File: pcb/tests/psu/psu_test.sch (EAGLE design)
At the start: 26 parts, among them J1 CUI-PJ-013C, J2 SNG-100-HEADER-05-HDR-V, J3 SNG-100-HEADER-04-HDR-V, J4 SNG-100-HEADER-03-HDR-V, U1 ADP2303ARDZ, U2 TPS62086RLT, U3 TS4040D30IDBZ

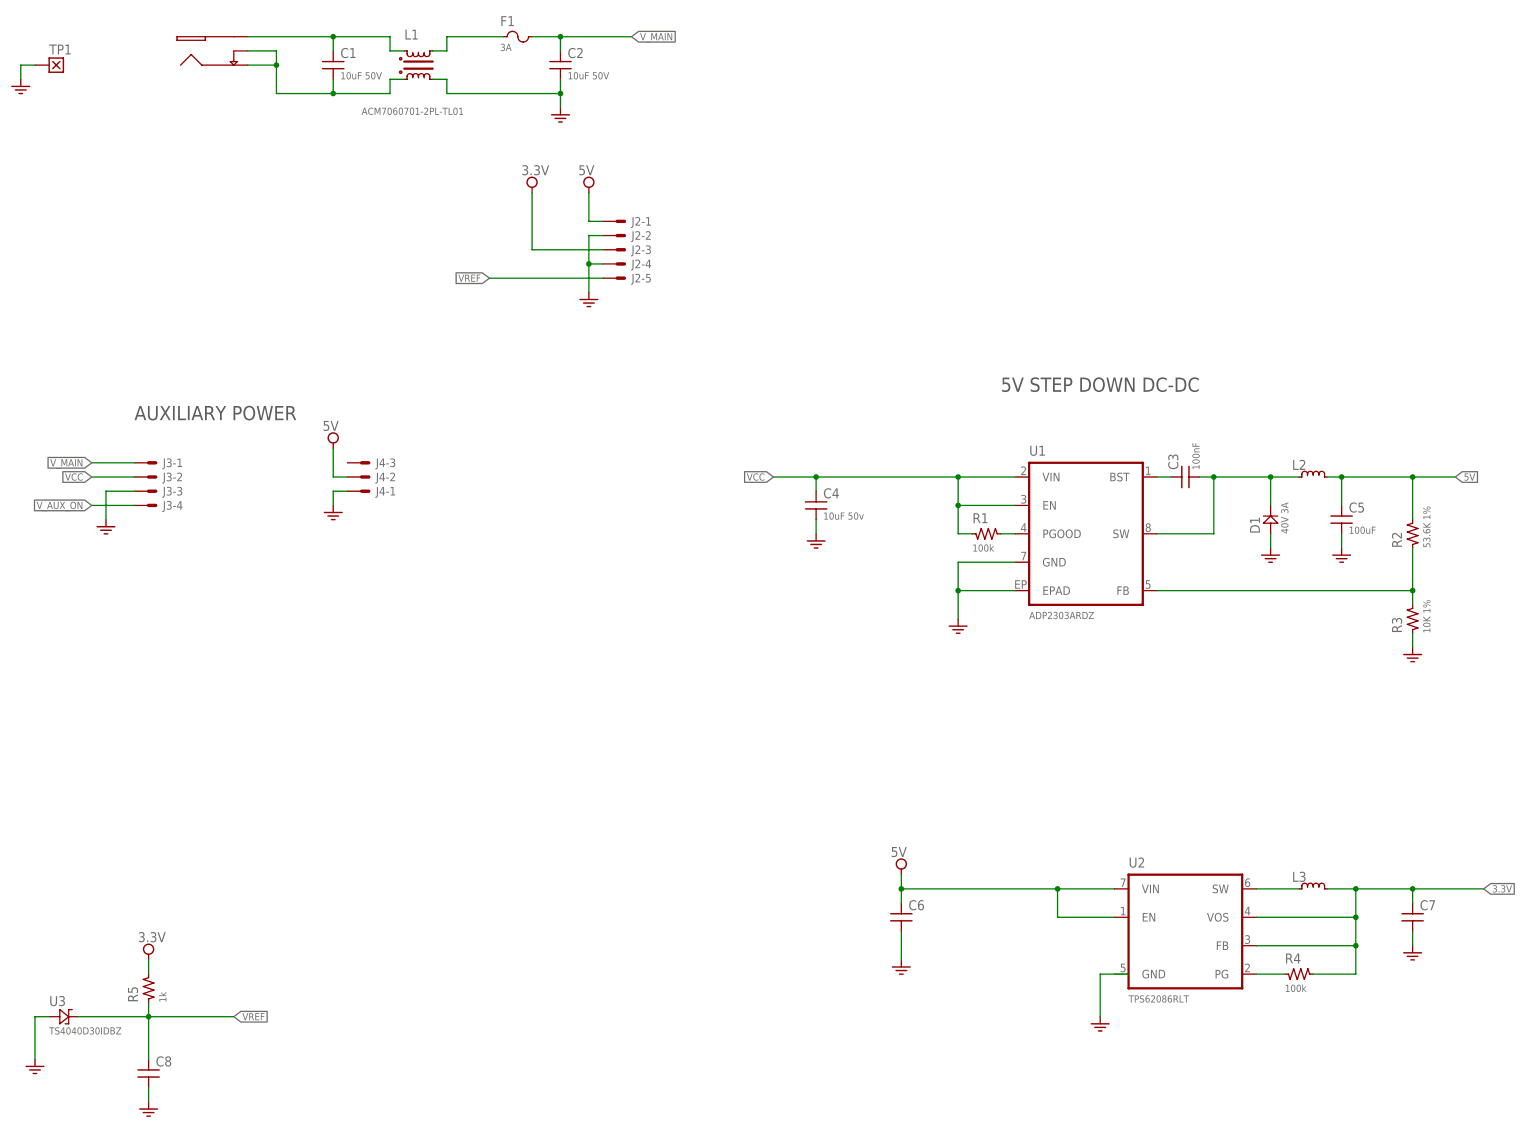
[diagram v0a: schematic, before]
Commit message: Corrected drawings of touch panel PCB
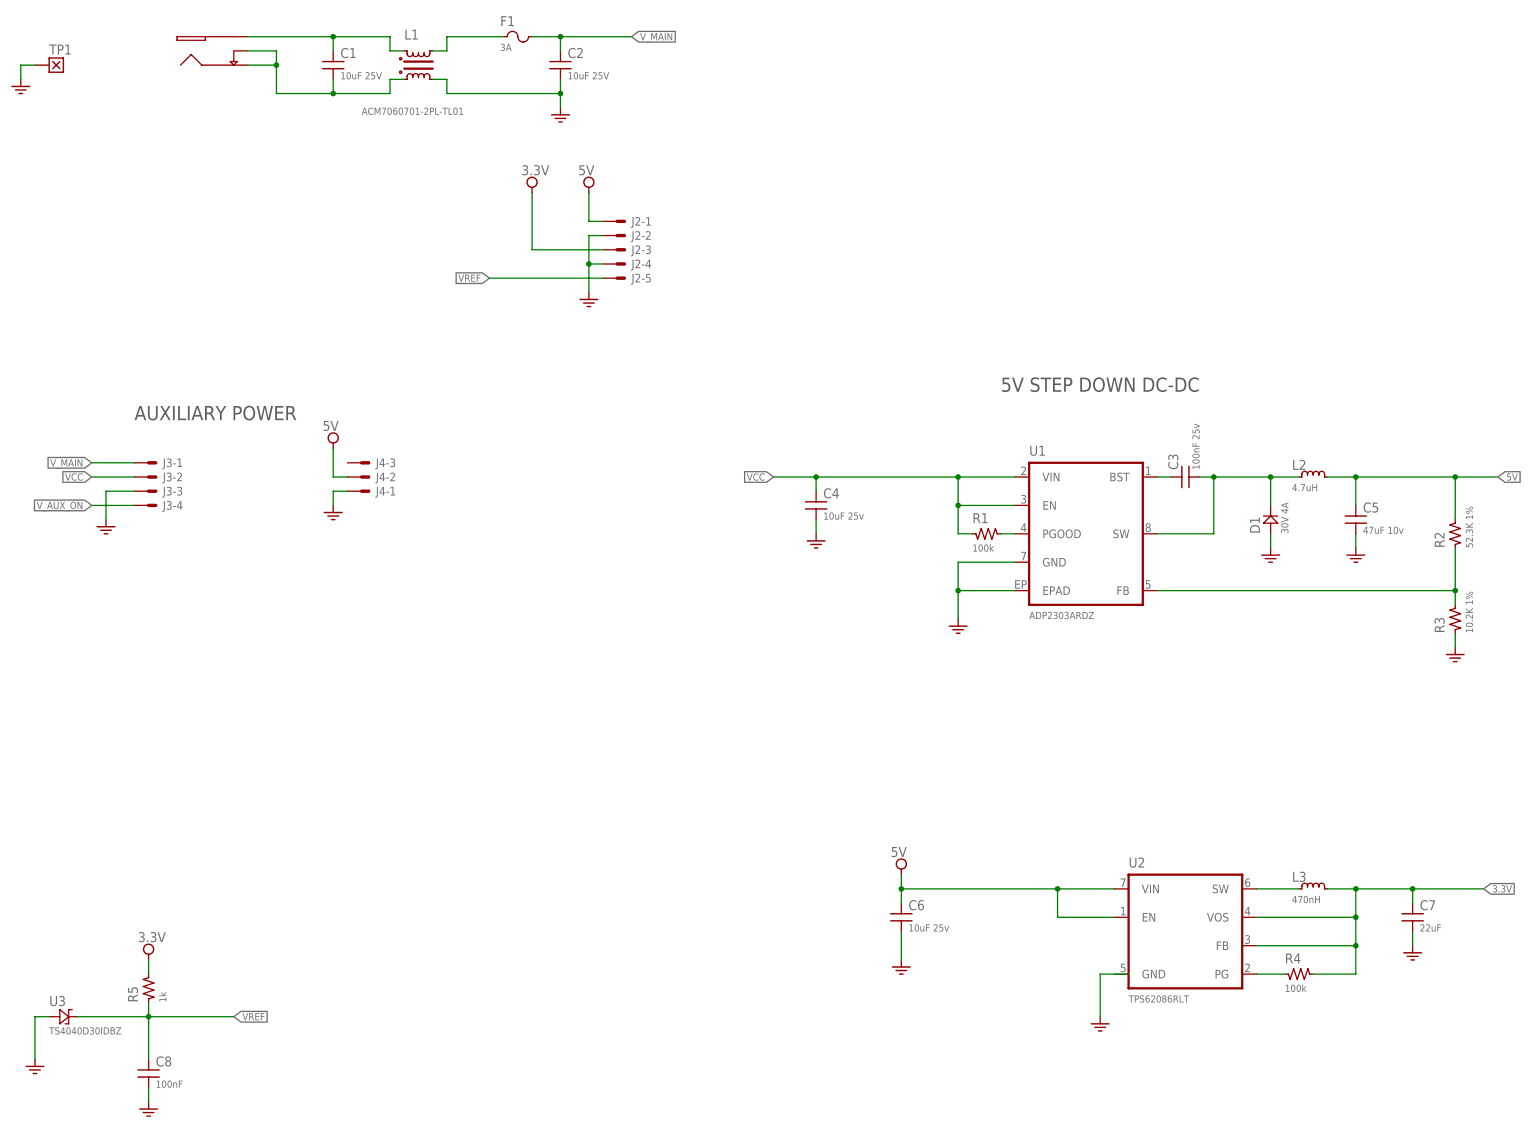
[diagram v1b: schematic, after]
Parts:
- C1, C2: value 10uF 50V -> 10uF 25V
- C3: value 100nF -> 100nF 25v
- C4: value 10uF 50v -> 10uF 25v
- C5: value 100uF -> 47uF 10v
- C6: value (none) -> 10uF 25v
- C7: value (none) -> 22uF
- C8: value (none) -> 100nF
- D1: value 40V 3A -> 30V 4A; MFG (none) -> Vishay Semiconductors; PART_NO (none) -> SSB43L-E3/52T; SKU (none) -> SSB43L-E3/52T
- L1: PART_NO (none) -> ACM7060-701-2PL-TL01
- L2: value (none) -> 4.7uH; device Passive:IND-74437324022 -> Passive:IND-4020; DESCRIPTION (none) -> {DESCRIPTION} - SMT 4020 - {VALUE}; MFG (none) -> TDK; PART_NO (none) -> CLF10040T-4R7N; SKU (none) -> CLF10040T-4R7N
- L3: value (none) -> 470nH
- R2: value 53.6K 1% -> 52.3K 1%
- R3: value 10K 1% -> 10.2K 1%
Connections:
- net 3.3V: now also L3.2; no longer L3.P$2
- net 5V: now also L2.2; no longer L2.P$2
- net N$33: now also L2.1; no longer L2.P$1
- net N$35: now also L3.1; no longer L3.P$1
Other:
- moved on the sheet: C5, R2, R3
